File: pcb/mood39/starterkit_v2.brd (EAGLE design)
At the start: 36 x 36 mm, 22 parts, among them IC1 TINY85, IC2 LP2950

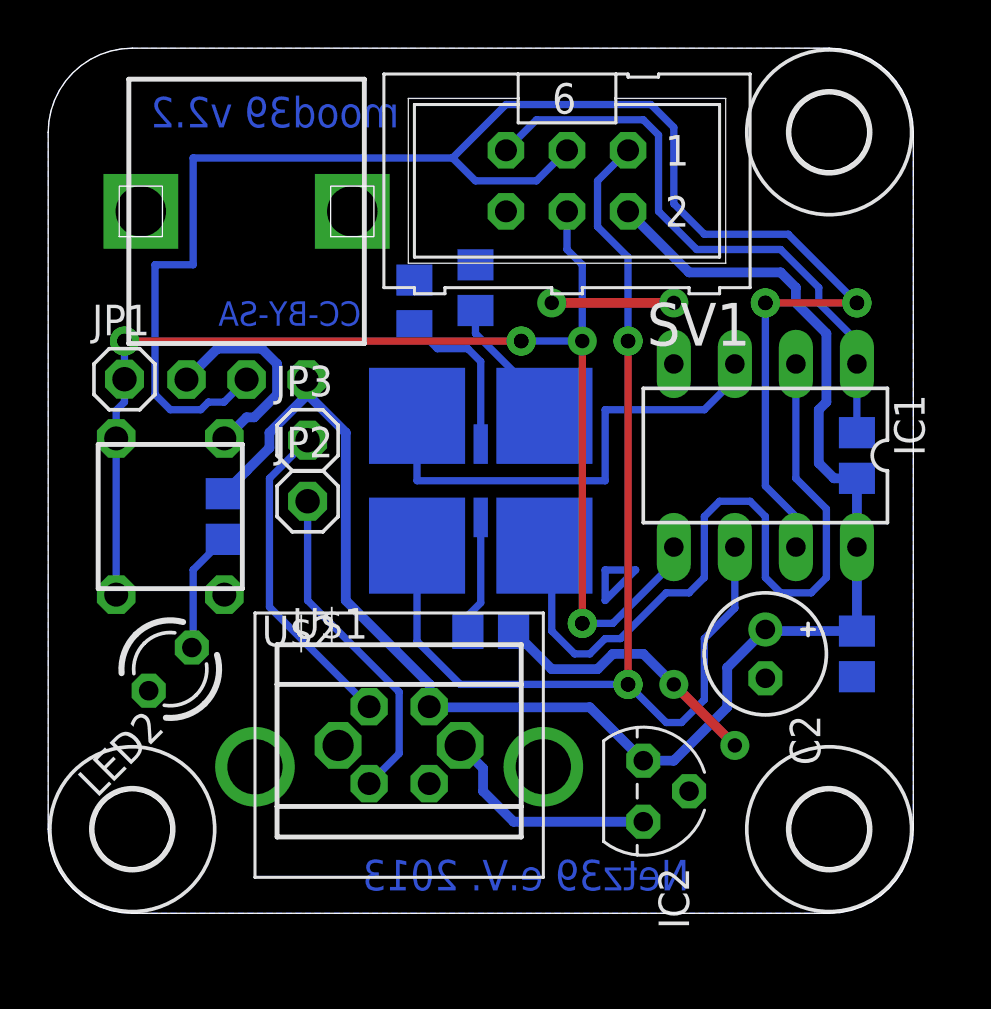
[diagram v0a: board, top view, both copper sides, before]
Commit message: optimize vias
removed double vias, moved some signals, did DRC again
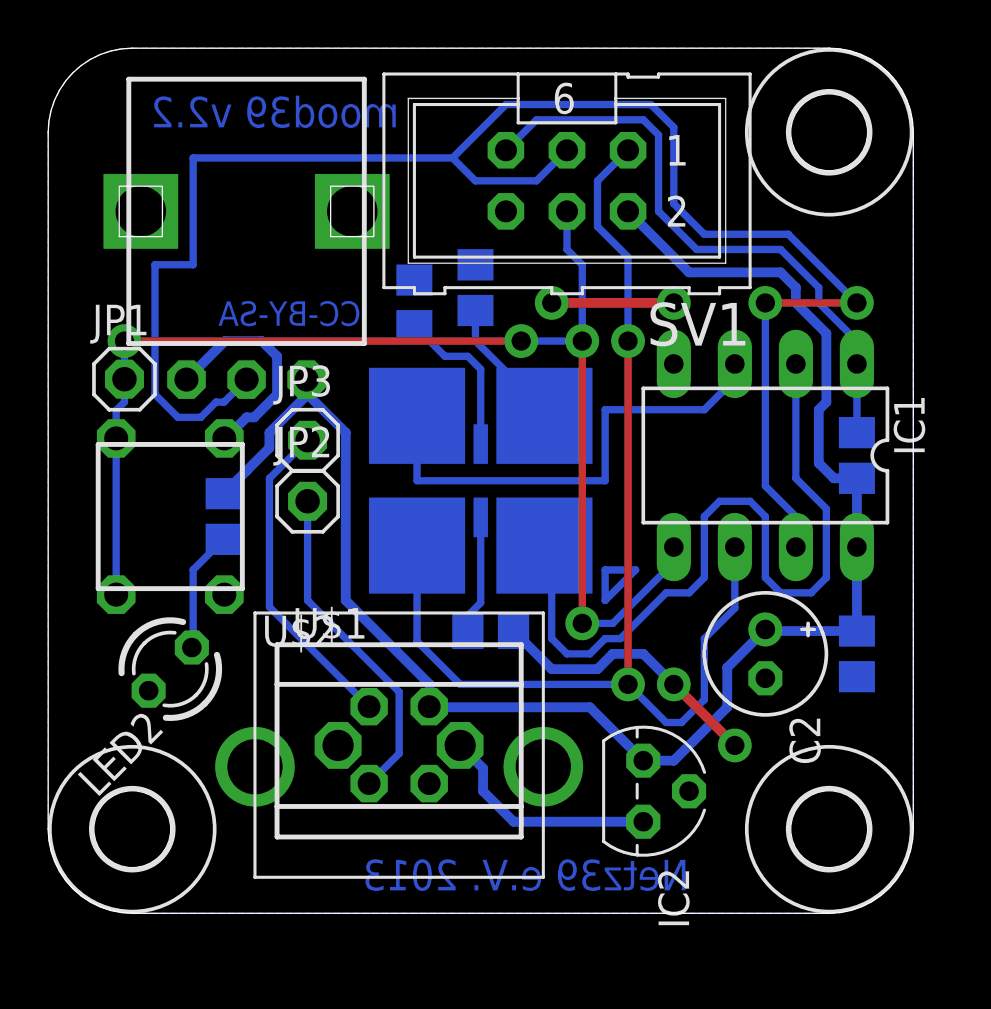
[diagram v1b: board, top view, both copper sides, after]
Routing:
- net MOSI: vias 7 -> 4
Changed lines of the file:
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@@
 <wire x1="15.35" y1="11.32" x2="17.145" y2="9.525" width="0.3048" layer="16"/>
 <wire x1="17.145" y1="9.525" x2="24.13" y2="9.525" width="0.3048" layer="16"/>
-<via x="24.13" y="9.525" extent="1-16" drill="0.6" shape="octagon"/>
+<via x="24.13" y="9.525" extent="1-16" drill="0.8" shape="octagon"/>
 <wire x1="24.13" y1="9.525" x2="24.13" y2="23.8125" width="0.3048" layer="1"/>
 <wire x1="28.575" y1="15.24" x2="28.575" y2="12.7" width="0.3048" layer="16"/>
@@
 <wire x1="22.86" y1="28.575" x2="24.13" y2="27.305" width="0.3048" layer="16"/>
 <wire x1="24.13" y1="27.305" x2="24.13" y2="23.8125" width="0.3048" layer="16"/>
-<via x="24.13" y="23.8125" extent="1-16" drill="0.6" shape="octagon"/>
+<via x="24.13" y="23.8125" extent="1-16" drill="0.8" shape="octagon"/>
 <wire x1="22.86" y1="30.48" x2="24.13" y2="31.75" width="0.3048" layer="16"/>
 </signal>
@@
 <wire x1="23.8125" y1="11.43" x2="23.1775" y2="11.43" width="0.3048" layer="16"/>
 <wire x1="23.1775" y1="11.43" x2="22.5425" y2="10.795" width="0.3048" layer="16"/>
-<wire x1="22.5425" y1="10.795" x2="21.9075" y2="10.795" width="0.3048" layer="16"/>
-<wire x1="21.9075" y1="10.795" x2="20.955" y2="11.7475" width="0.3048" layer="16"/>
+<wire x1="22.5425" y1="10.795" x2="21.59" y2="10.795" width="0.3048" layer="16"/>
 <wire x1="20.65" y1="15.3" x2="20.955" y2="14.995" width="0.3048" layer="16"/>
-<wire x1="20.955" y1="14.995" x2="20.955" y2="11.7475" width="0.3048" layer="16"/>
+<wire x1="20.955" y1="14.995" x2="20.955" y2="11.43" width="0.3048" layer="16"/>
+<wire x1="21.59" y1="10.795" x2="20.955" y2="11.43" width="0.3048" layer="16"/>
 </signal>
 <signal name="GND" class="1">
@@
 <contactref element="U$2" pad="4"/>
 <contactref element="R5" pad="1"/>
-<via x="26.035" y="9.525" extent="1-16" drill="0.6" shape="octagon"/>
-<via x="28.575" y="6.985" extent="1-16" drill="0.6" shape="octagon"/>
+<via x="26.035" y="9.525" extent="1-16" drill="0.8" shape="octagon"/>
+<via x="28.575" y="6.985" extent="1-16" drill="0.8" shape="octagon"/>
 <wire x1="26.035" y1="9.525" x2="24.765" y2="10.795" width="0.4064" layer="16"/>
 <wire x1="24.765" y1="10.795" x2="23.495" y2="10.795" width="0.4064" layer="16"/>
@@
 <wire x1="20.9525" y1="10.16" x2="19.365" y2="11.7475" width="0.4064" layer="16"/>
 <wire x1="26.035" y1="9.525" x2="28.575" y2="6.985" width="0.4064" layer="1"/>
-<wire x1="9.525" y1="21.59" x2="9.525" y2="22.86" width="0.4064" layer="16"/>
-<wire x1="9.525" y1="22.86" x2="8.89" y2="23.495" width="0.4064" layer="16"/>
-<wire x1="8.89" y1="23.495" x2="7.04" y2="23.495" width="0.4064" layer="16"/>
-<wire x1="7.04" y1="23.495" x2="5.755" y2="22.21" width="0.4064" layer="16"/>
+<wire x1="9.525" y1="21.59" x2="9.525" y2="23.1775" width="0.4064" layer="16"/>
+<wire x1="7.3575" y1="23.8125" x2="5.755" y2="22.21" width="0.4064" layer="16"/>
 <wire x1="7.33" y1="19.76" x2="7.3775" y2="19.76" width="0.4064" layer="16"/>
 <wire x1="7.3775" y1="19.76" x2="8.255" y2="20.6375" width="0.4064" layer="16"/>
 <wire x1="8.255" y1="20.6375" x2="8.5725" y2="20.6375" width="0.4064" layer="16"/>
 <wire x1="8.5725" y1="20.6375" x2="9.525" y2="21.59" width="0.4064" layer="16"/>
-<via x="26.035" y="25.4" extent="1-16" drill="0.6" shape="octagon"/>
-<via x="20.955" y="25.4" extent="1-16" drill="0.6" shape="octagon"/>
+<via x="26.035" y="25.4" extent="1-16" drill="0.8" shape="octagon"/>
+<via x="20.955" y="25.4" extent="1-16" drill="0.8" shape="octagon"/>
 <wire x1="20.955" y1="25.4" x2="26.035" y2="25.4" width="0.4064" layer="1"/>
 <polygon width="0.4064" layer="16" thermals="no">
@@
 <vertex x="0" y="3.5" curve="90"/>
 </polygon>
+<wire x1="7.3575" y1="23.8125" x2="8.89" y2="23.8125" width="0.4064" layer="16"/>
+<wire x1="9.525" y1="23.1775" x2="8.89" y2="23.8125" width="0.4064" layer="16"/>
 </signal>
 <signal name="VCC" class="1">
@@
 <contactref element="LED1" pad="5"/>
 <contactref element="R2" pad="1"/>
-<wire x1="18" y1="19.525" x2="18" y2="22.9575" width="0.3048" layer="16"/>
-<wire x1="18" y1="22.9575" x2="17.4625" y2="23.495" width="0.3048" layer="16"/>
-<wire x1="17.4625" y1="23.495" x2="16.195" y2="23.495" width="0.3048" layer="16"/>
-<wire x1="16.195" y1="23.495" x2="15.24" y2="24.45" width="0.3048" layer="16"/>
+<wire x1="16.5125" y1="23.1775" x2="15.24" y2="24.45" width="0.3048" layer="16"/>
+<wire x1="18" y1="19.525" x2="18" y2="22.64" width="0.3048" layer="16"/>
+<wire x1="18" y1="22.64" x2="17.4625" y2="23.1775" width="0.3048" layer="16"/>
+<wire x1="17.4625" y1="23.1775" x2="16.5125" y2="23.1775" width="0.3048" layer="16"/>
 </signal>
 <signal name="N$6" class="2">
@@
 <contactref element="LED1" pad="6"/>
 <contactref element="R4" pad="1"/>
-<wire x1="17.78" y1="25.085" x2="17.78" y2="24.13" width="0.3048" layer="16"/>
-<wire x1="17.78" y1="24.13" x2="19.3675" y2="22.5425" width="0.3048" layer="16"/>
-<wire x1="19.3675" y1="22.5425" x2="19.3675" y2="21.9825" width="0.3048" layer="16"/>
+<wire x1="17.78" y1="25.085" x2="17.78" y2="23.8125" width="0.3048" layer="16"/>
+<wire x1="17.78" y1="23.8125" x2="19.3675" y2="22.225" width="0.3048" layer="16"/>
+<wire x1="19.3675" y1="22.225" x2="19.3675" y2="21.9825" width="0.3048" layer="16"/>
 <wire x1="19.3675" y1="21.9825" x2="20.65" y2="20.7" width="0.3048" layer="16"/>
 </signal>
@@
 <contactref element="SV1" pad="3"/>
 <contactref element="R5" pad="2"/>
-<wire x1="6.35" y1="20.955" x2="5.08" y2="20.955" width="0.3048" layer="16"/>
-<wire x1="5.08" y1="20.955" x2="4.445" y2="21.59" width="0.3048" layer="16"/>
+<wire x1="5.3975" y1="20.6375" x2="4.445" y2="21.59" width="0.3048" layer="16"/>
 <wire x1="20.32" y1="30.48" x2="17.78" y2="30.48" width="0.3048" layer="16"/>
 <wire x1="16.8275" y1="31.4325" x2="6.0325" y2="31.4325" width="0.3048" layer="16"/>
@@
 <wire x1="6.0325" y1="26.9875" x2="4.445" y2="26.9875" width="0.3048" layer="16"/>
 <wire x1="4.445" y1="26.9875" x2="4.445" y2="21.59" width="0.3048" layer="16"/>
-<wire x1="6.35" y1="20.955" x2="6.6675" y2="21.2725" width="0.3048" layer="16"/>
-<wire x1="6.6675" y1="21.2725" x2="7.3175" y2="21.2725" width="0.3048" layer="16"/>
 <wire x1="7.3175" y1="21.2725" x2="8.255" y2="22.21" width="0.3048" layer="16"/>
 <wire x1="31.115" y1="15.24" x2="31.115" y2="16.51" width="0.3048" layer="16"/>
 <wire x1="31.115" y1="16.51" x2="29.845" y2="17.78" width="0.3048" layer="16"/>
 <wire x1="29.845" y1="17.78" x2="29.845" y2="25.4" width="0.3048" layer="16"/>
-<via x="29.845" y="25.4" extent="1-16" drill="0.6" shape="octagon"/>
+<via x="29.845" y="25.4" extent="1-16" drill="0.8" shape="octagon"/>
 <wire x1="29.845" y1="25.4" x2="33.655" y2="25.4" width="0.3048" layer="1"/>
-<via x="33.655" y="25.4" extent="1-16" drill="0.6" shape="octagon"/>
+<via x="33.655" y="25.4" extent="1-16" drill="0.8" shape="octagon"/>
 <wire x1="19.05" y1="33.655" x2="16.8275" y2="31.4325" width="0.3048" layer="16"/>
 <wire x1="17.78" y1="30.48" x2="16.8275" y2="31.4325" width="0.3048" layer="16"/>
@@
 <wire x1="25.0825" y1="33.655" x2="19.05" y2="33.655" width="0.3048" layer="16"/>
 <wire x1="33.655" y1="25.4" x2="30.7975" y2="28.2575" width="0.3048" layer="16"/>
+<wire x1="5.3975" y1="20.6375" x2="6.35" y2="20.6375" width="0.3048" layer="16"/>
+<wire x1="6.35" y1="20.6375" x2="6.985" y2="21.2725" width="0.3048" layer="16"/>
+<wire x1="6.985" y1="21.2725" x2="7.3175" y2="21.2725" width="0.3048" layer="16"/>
 </signal>
 <signal name="MOSI" class="2">
@@
 <wire x1="2.83" y1="19.76" x2="2.83" y2="13.26" width="0.3048" layer="16"/>
 <wire x1="3.175" y1="22.225" x2="3.175" y2="23.8125" width="0.3048" layer="16"/>
-<via x="3.175" y="23.8125" extent="1-16" drill="0.6" shape="octagon"/>
 <wire x1="3.175" y1="23.8125" x2="19.685" y2="23.8125" width="0.3048" layer="1"/>
-<via x="19.685" y="23.8125" extent="1-16" drill="0.6" shape="octagon"/>
 <wire x1="19.685" y1="23.8125" x2="22.225" y2="23.8125" width="0.3048" layer="16"/>
 <wire x1="26.035" y1="15.24" x2="26.035" y2="14.605" width="0.3048" layer="16"/>
 <wire x1="26.035" y1="14.605" x2="23.495" y2="12.065" width="0.3048" layer="16"/>
 <wire x1="23.495" y1="12.065" x2="22.225" y2="12.065" width="0.3048" layer="16"/>
-<via x="22.225" y="12.065" extent="1-16" drill="0.6" shape="octagon"/>
 <wire x1="22.225" y1="12.065" x2="22.225" y2="23.8125" width="0.3048" layer="1"/>
-<via x="22.225" y="23.8125" extent="1-16" drill="0.6" shape="octagon"/>
-<via x="19.685" y="23.8125" extent="1-16" drill="0.6" shape="octagon"/>
-<via x="3.175" y="23.8125" extent="1-16" drill="0.6" shape="octagon"/>
-<via x="22.225" y="12.065" extent="1-16" drill="0.6" shape="octagon"/>
+<via x="22.225" y="23.8125" extent="1-16" drill="0.8" shape="octagon"/>
+<via x="19.685" y="23.8125" extent="1-16" drill="0.8" shape="octagon"/>
+<via x="3.175" y="23.8125" extent="1-16" drill="0.8" shape="octagon"/>
+<via x="22.225" y="12.065" extent="1-16" drill="0.8" shape="octagon"/>
 <wire x1="21.59" y1="29.21" x2="21.59" y2="27.6225" width="0.3048" layer="16"/>
 <wire x1="21.59" y1="27.6225" x2="22.225" y2="26.9875" width="0.3048" layer="16"/>
@@
 </signal>
 <signal name="N$9">
-<via x="24.13" y="23.8125" extent="1-16" drill="0.6" shape="octagon"/>
 </signal>
 <signal name="N$15">
-<via x="24.13" y="9.525" extent="1-16" drill="0.6" shape="octagon"/>
 </signal>
 <signal name="N$19">
 </signal>
 <signal name="N$3">
-<via x="29.845" y="25.4" extent="1-16" drill="0.6" shape="octagon"/>
 </signal>
 <signal name="N$4">
-<via x="33.655" y="25.4" extent="1-16" drill="0.6" shape="octagon"/>
 </signal>
 <signal name="N$16">

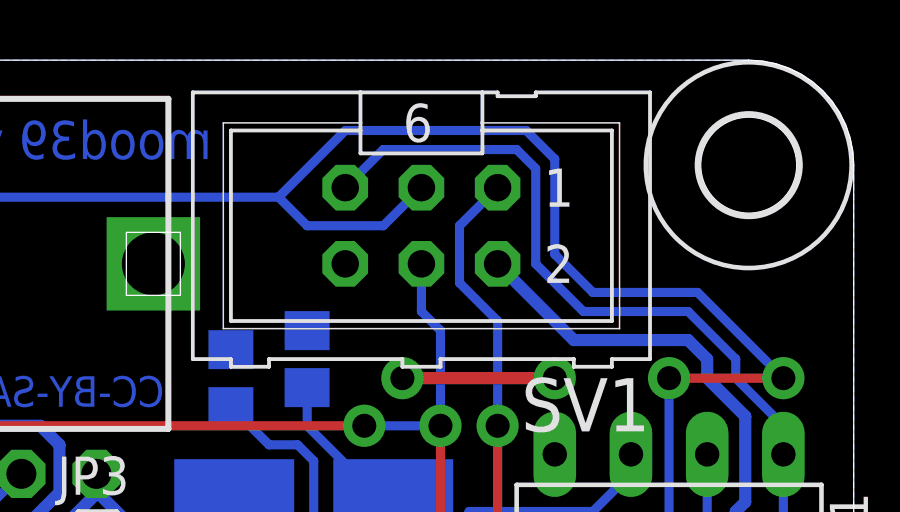
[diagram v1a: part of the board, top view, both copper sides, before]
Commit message: square pad for ISP pin 1 and add documentation
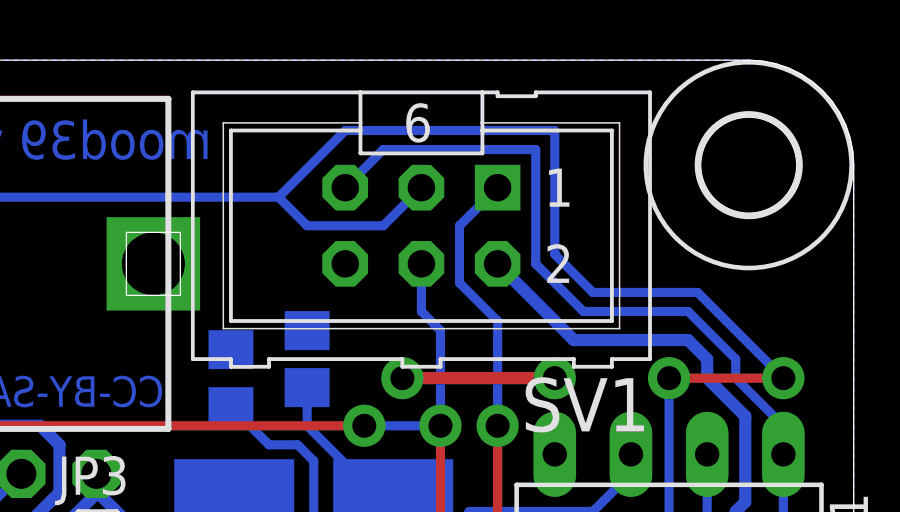
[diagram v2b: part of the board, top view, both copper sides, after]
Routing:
- net SCK: track 70.3 -> 70.8 mm
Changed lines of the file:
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@@
 <layer number="21" name="tPlace" color="7" fill="1" visible="yes" active="yes"/>
 <layer number="22" name="bPlace" color="7" fill="1" visible="yes" active="yes"/>
-<layer number="23" name="tOrigins" color="15" fill="1" visible="no" active="yes"/>
-<layer number="24" name="bOrigins" color="15" fill="1" visible="no" active="yes"/>
+<layer number="23" name="tOrigins" color="15" fill="1" visible="yes" active="yes"/>
+<layer number="24" name="bOrigins" color="15" fill="1" visible="yes" active="yes"/>
 <layer number="25" name="tNames" color="7" fill="1" visible="no" active="yes"/>
 <layer number="26" name="bNames" color="7" fill="1" visible="no" active="yes"/>
 <layer number="27" name="tValues" color="7" fill="1" visible="no" active="yes"/>
-<layer number="28" name="bValues" color="7" fill="1" visible="yes" active="yes"/>
+<layer number="28" name="bValues" color="7" fill="1" visible="no" active="yes"/>
 <layer number="29" name="tStop" color="7" fill="3" visible="no" active="yes"/>
 <layer number="30" name="bStop" color="7" fill="6" visible="no" active="yes"/>
@@
 <wire x1="30.7975" y1="28.2575" x2="27.305" y2="28.2575" width="0.3048" layer="16"/>
 <wire x1="27.305" y1="28.2575" x2="26.035" y2="29.5275" width="0.3048" layer="16"/>
-<wire x1="26.035" y1="29.5275" x2="26.035" y2="32.7025" width="0.3048" layer="16"/>
-<wire x1="26.035" y1="32.7025" x2="25.0825" y2="33.655" width="0.3048" layer="16"/>
-<wire x1="25.0825" y1="33.655" x2="19.05" y2="33.655" width="0.3048" layer="16"/>
+<wire x1="26.035" y1="29.5275" x2="26.035" y2="33.655" width="0.3048" layer="16"/>
+<wire x1="26.035" y1="33.655" x2="19.05" y2="33.655" width="0.3048" layer="16"/>
 <wire x1="33.655" y1="25.4" x2="30.7975" y2="28.2575" width="0.3048" layer="16"/>
 <wire x1="5.3975" y1="20.6375" x2="6.35" y2="20.6375" width="0.3048" layer="16"/>
@@
 <wire x1="33.655" y1="22.86" x2="33.655" y2="23.8125" width="0.3048" layer="16"/>
 <wire x1="33.655" y1="23.8125" x2="32.0675" y2="25.4" width="0.3048" layer="16"/>
-<wire x1="20.32" y1="33.02" x2="24.765" y2="33.02" width="0.3048" layer="16"/>
-<wire x1="24.765" y1="33.02" x2="25.4" y2="32.385" width="0.3048" layer="16"/>
-<wire x1="25.4" y1="32.385" x2="25.4" y2="29.21" width="0.3048" layer="16"/>
+<wire x1="20.32" y1="33.02" x2="25.4" y2="33.02" width="0.3048" layer="16"/>
+<wire x1="25.4" y1="33.02" x2="25.4" y2="29.21" width="0.3048" layer="16"/>
 <wire x1="25.4" y1="29.21" x2="26.9875" y2="27.6225" width="0.3048" layer="16"/>
 <wire x1="26.9875" y1="27.6225" x2="30.48" y2="27.6225" width="0.3048" layer="16"/>

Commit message: target #9
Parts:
- JP2: value (none) -> USBD+
- JP3: value (none) -> USBD-
- S1: value (none) -> TASTER 9305
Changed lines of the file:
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@@
 <element name="LED2" library="led" package="LED3MM" value="rot lc" x="5.08" y="10.16" rot="R225"/>
 <element name="R6" library="rcl" package="R0805" value="1.5k" x="7.3025" y="16.51" rot="MR270"/>
-<element name="S1" library="n39" package="JTP-1130" value="" x="5.08" y="16.51" rot="R90">
+<element name="S1" library="n39" package="JTP-1130" value="TASTER 9305" x="5.08" y="16.51" rot="R90">
 <attribute name="REICHELT" value="TASTER 9305" x="5.08" y="16.51" size="1.778" layer="27" rot="R90" display="off"/>
 </element>
@@
 <attribute name="REICHELT" value="AKL 101-02" x="14.605" y="6.985" size="1.778" layer="27" display="off"/>
 </element>
-<element name="JP2" library="pinhead" package="1X01" value="" x="10.795" y="17.145"/>
-<element name="JP3" library="pinhead" package="1X01" value="" x="10.795" y="19.685"/>
+<element name="JP2" library="pinhead" package="1X01" value="USBD+" x="10.795" y="17.145"/>
+<element name="JP3" library="pinhead" package="1X01" value="USBD-" x="10.795" y="19.685"/>
 <element name="U$2" library="n39" package="USB_B_UP-S" value="USB_BS" x="14.605" y="5.3975">
 <attribute name="REICHELT" value="USB BG" x="14.605" y="5.3975" size="1.778" layer="27" display="off"/>
